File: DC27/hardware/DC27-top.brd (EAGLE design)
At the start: 102.4 x 117.6 mm, 44 parts, among them IC1 PCA9956BTWY

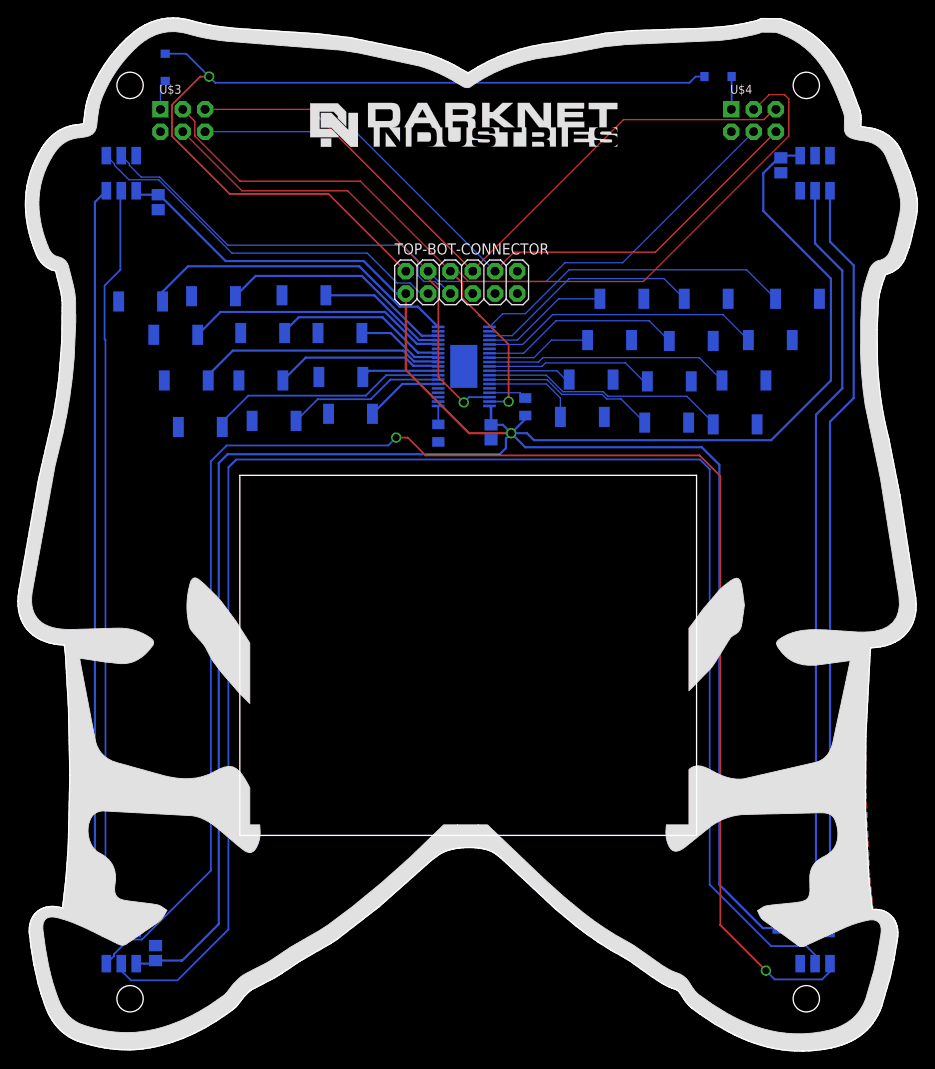
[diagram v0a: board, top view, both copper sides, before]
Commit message: removed apa 102s from top board swapped led driver for atmega4089 put on programming pads bottom board adding paring headers on bottom board added 1206 56 OHM resistors to each LED top board pulled out UPDI pin on top board for programming the atmega chip
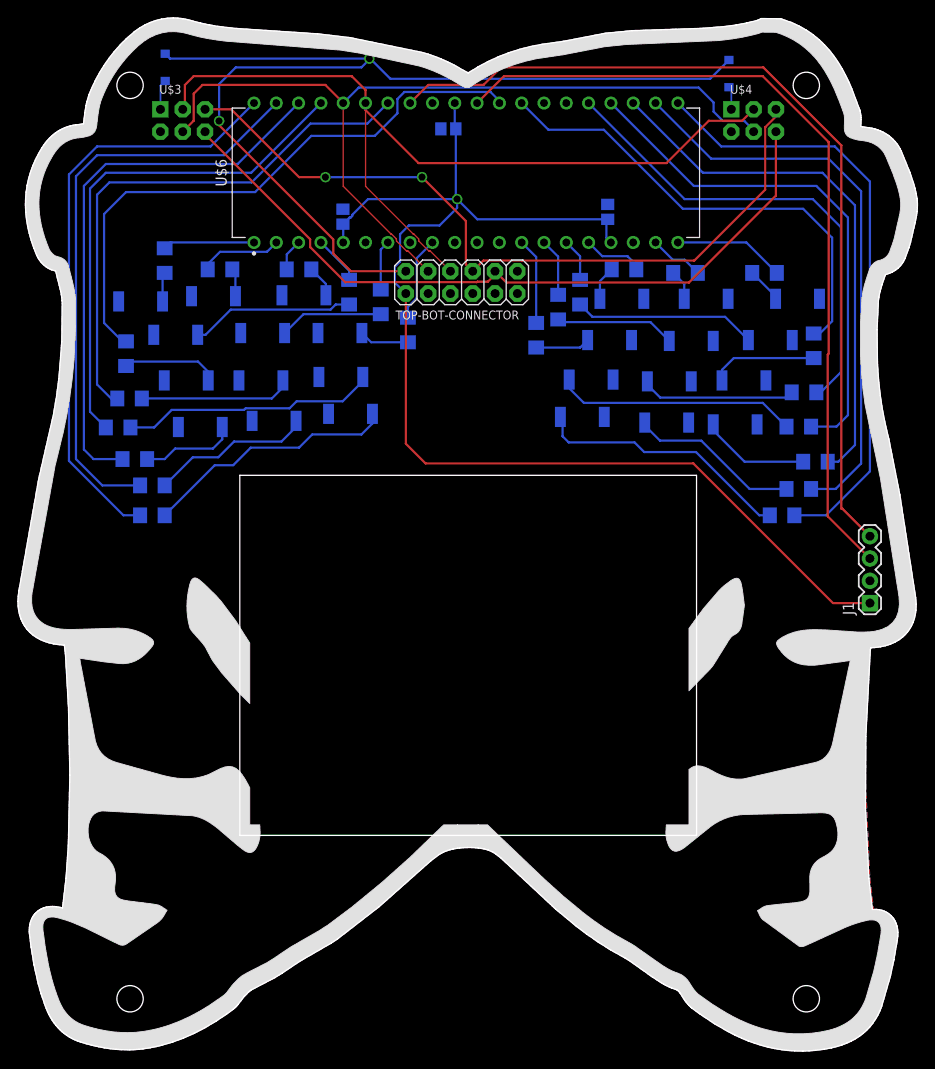
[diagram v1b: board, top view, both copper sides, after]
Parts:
- removed C26, C27, C28, C29: 15 pF, passives:C0805
- removed IC1: PCA9956BTWY, PCA9956BTWY:SOP50P640X110-39N
- removed U$11, U$12, U$13, U$14: APA1025050, leds:APA102_5050
- added C2, C3: 0.1 uF, passives:C0805
- added J1: (no value), connector:1X04
- added R1, R10, R11, R12, R13, R14, R15, R16, R17, R18, R19, R20, R21, R22, R23, R24, R3, R4, R5, R6, R8, R9: 56 R, passives:1206
- added U$6: ATMEGA4809-PFATMEL4809-PF, ICs:DIP1587W58P254L5175H635Q40B
- LED1, LED10, LED11, LED12, LED13, LED14, LED15, LED16, LED17, LED18, LED19, LED2, LED20, LED21, LED22, LED23, LED24, LED3, LED4, LED5, LED6, LED7, LED8, LED9: value (none) -> Amber
- R2: value 10 K -> 56 R; device darknet_parts_library:R0805 -> passives:1206
- R7: value 2 K -> 56 R; device darknet_parts_library:R0805 -> passives:1206
- moved R2 43.4 mm to (15.3, 64.4), turned to 0 degrees
- moved C1 28.4 mm to (67.1, 95.5), turned to 270 degrees
- moved R7 12.2 mm to (44.4, 82.1), turned to 90 degrees
- moved U$5 5.10 mm to (51.8, 100.5), flipped to the bottom
- moved D1 1.23 mm to (81.0, 111.2), turned to 270 degrees
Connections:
- removed net APA102_CLK: TOP-BOT-CONNECTOR.5, U$13.5
- removed net APA102_DATA: TOP-BOT-CONNECTOR.3, U$13.4
- new net N$28: LED6.A, R6.1
- new net N$30: LED18.A, R18.2
- new net N$31: LED1.A, R1.1
- new net N$32: LED2.A, R2.1
- new net N$33: R17.1, U$6.14
- new net N$40: LED22.A, R22.1
- new net N$41: LED19.A, R19.1
- new net N$42: LED21.A, R21.1
- new net N$43: LED20.A, R20.1
- new net N$44: R19.2, U$6.28
- new net N$45: R20.2, U$6.25
- new net N$46: R21.2, U$6.24
- new net N$47: R22.2, U$6.23
- new net N$48: R23.2, U$6.22
- new net N$49: R24.2, U$6.21
- new net N$51: LED3.A, R3.2
- new net PA0: J1.4, U$6.33
- new net PC5: U$6.8
- new net PD1: U$6.10
- new net PD2: U$6.11
- new net PD3: U$6.12
- new net PF3: U$6.26
- new net PF4: U$6.27
- new net UPDI: J1.3, U$6.30
- net GND: now also C2.1, C3.1, J1.2, U$6.18, U$6.32, U$6.6; no longer C26.2, C27.2, C28.2, C29.2, IC1.14, IC1.18, IC1.2, IC1.21, IC1.25, IC1.3, IC1.34, IC1.39, IC1.5, R7.2, U$11.6, U$12.6, U$13.6, U$14.6
- net N$1: now also R9.2, U$6.4; no longer IC1.6, LED1.A
- net N$10: now also R10.1, U$6.3; no longer IC1.16, LED10.A
- net N$11: now also R11.2, U$6.2; no longer IC1.17, LED11.A
- net N$12: now also R12.2, U$6.1; no longer IC1.19, LED12.A
- net N$13: now also R4.2, U$6.37; no longer IC1.20, LED13.A
- net N$14: now also LED5.A, R5.1; no longer IC1.22, LED14.A
- net N$15: now also R5.2, U$6.34; no longer IC1.23, LED15.A
- net N$16: now also R13.1, U$6.20; no longer IC1.24, LED16.A
- net N$17: now also LED13.A, R13.2; no longer IC1.26, LED17.A
- net N$18: now also R14.1, U$6.19; no longer IC1.27, LED18.A
- net N$19: now also LED14.A, R14.2; no longer IC1.28, LED19.A
- net N$2: now also LED9.A, R9.1; no longer IC1.7, LED2.A
- net N$20: now also R15.1, U$6.16; no longer IC1.29, LED20.A
- net N$21: now also LED15.A, R15.2; no longer IC1.30, LED21.A
- net N$22: now also LED17.A, R17.2; no longer IC1.31, LED22.A
- net N$23: now also LED16.A, R16.2; no longer IC1.32, LED23.A
- net N$24: now also R18.1, U$6.13; no longer IC1.33, LED24.A
- net N$27: now also R6.2, U$6.29; no longer U$11.4, U$12.3
- net N$29: now also LED4.A, R4.1; no longer U$12.5, U$14.2
- net N$3: now also R8.2, U$6.7; no longer IC1.8, LED3.A
- net N$34: now also R16.1, U$6.15; no longer U$11.5, U$12.2
- net N$35: now also LED24.A, R24.1; no longer IC1.1, R7.1
- net N$36: now also LED10.A, R10.2; no longer IC1.35, R2.2
- net N$37: now also LED11.A, R11.1; no longer U$12.4, U$14.3
- net N$38: now also LED12.A, R12.1; no longer U$13.3, U$14.4
- net N$39: now also LED23.A, R23.1; no longer U$13.2, U$14.5
- net N$4: now also R7.2, U$6.9; no longer IC1.9, LED4.A
- net N$5: now also R1.2, U$6.40; no longer IC1.10, LED5.A
- net N$6: now also R2.2, U$6.39; no longer IC1.11, LED6.A
- net N$7: now also R3.1, U$6.38; no longer IC1.12, LED7.A
- net N$8: now also R8.1; no longer IC1.13
- net N$9: now also LED7.A, R7.1; no longer IC1.15, LED9.A
- net SCL: now also U$6.36; no longer IC1.36
- net SDA: now also U$6.35; no longer IC1.37
- net VBAT: now also C2.2, C3.2, J1.1, U$6.17, U$6.31, U$6.5; no longer C26.1, C27.1, C28.1, C29.1, IC1.38, R2.1, U$11.1, U$12.1, U$13.1, U$14.1
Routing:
- net N$37: track 191.4 -> 3.20 mm, vias 2 -> 0
- net VBAT: track 321.6 -> 142.2 mm
- net N$29: track 187.7 -> 29.1 mm
- net PA0: track 0.00 -> 100.4 mm
- net UPDI: track 0.00 -> 93.9 mm
- net N$38: track 85.1 -> 3.35 mm
- net N$34: track 86.6 -> 4.91 mm
- net N$49: track 0.00 -> 69.2 mm
- net N$39: track 85.6 -> 19.4 mm
- net N$48: track 0.00 -> 65.5 mm
- net N$47: track 0.00 -> 61.3 mm
- net N$46: track 0.00 -> 59.6 mm
- net N$45: track 0.00 -> 54.8 mm
- net N$44: track 0.00 -> 53.9 mm
- net N$7: track 9.83 -> 63.2 mm
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
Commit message: tweaked position of the led 7 and 8 to be at same Y as the right eye (+/- .1 mm) rerouted trace so it does not go between resistor on bottom board
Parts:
- moved R12 1.48 mm to (16.0, 88.7), turned to 0 degrees
- moved LED8 0.92 mm to (25.2, 79.4)
- moved LED7 0.71 mm to (34.3, 79.6)
- moved LED9 0.60 mm to (15.5, 79.5)
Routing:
- net N$12: track 10.4 -> 14.2 mm
- net N$8: track 11.8 -> 12.4 mm
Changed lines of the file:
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@@
 <layer number="27" name="tValues" color="7" fill="1" visible="no" active="yes"/>
 <layer number="28" name="bValues" color="7" fill="1" visible="no" active="yes"/>
-<layer number="29" name="tStop" color="7" fill="3" visible="no" active="yes"/>
+<layer number="29" name="tStop" color="7" fill="3" visible="yes" active="yes"/>
 <layer number="30" name="bStop" color="7" fill="6" visible="no" active="yes"/>
 <layer number="31" name="tCream" color="7" fill="4" visible="no" active="yes"/>
@@
 <element name="LED5" library="leds" package="GULLWING_LED" value="Amber" x="25.158228125" y="74.850259375" smashed="yes" rot="MR180"/>
 <element name="LED6" library="leds" package="GULLWING_LED" value="Amber" x="16.658228125" y="74.850259375" smashed="yes" rot="MR180"/>
-<element name="LED7" library="leds" package="GULLWING_LED" value="Amber" x="34.158228125" y="80.250259375" smashed="yes" rot="MR180"/>
-<element name="LED8" library="leds" package="GULLWING_LED" value="Amber" x="25.358228125" y="80.250259375" smashed="yes" rot="MR180"/>
-<element name="LED9" library="leds" package="GULLWING_LED" value="Amber" x="15.458228125" y="80.050259375" smashed="yes" rot="MR180"/>
+<element name="LED7" library="leds" package="GULLWING_LED" value="Amber" x="34.258228125" y="79.550259375" smashed="yes" rot="MR180"/>
+<element name="LED8" library="leds" package="GULLWING_LED" value="Amber" x="25.158228125" y="79.350259375" smashed="yes" rot="MR180"/>
+<element name="LED9" library="leds" package="GULLWING_LED" value="Amber" x="15.458228125" y="79.450259375" smashed="yes" rot="MR180"/>
 <element name="LED10" library="leds" package="GULLWING_LED" value="Amber" x="30.058228125" y="84.550259375" smashed="yes" rot="MR180"/>
 <element name="LED11" library="leds" package="GULLWING_LED" value="Amber" x="19.758228125" y="84.450259375" smashed="yes" rot="MR180"/>
@@
 <attribute name="VALUE" x="24.397" y="87.476" size="0.4064" layer="28" rot="MR0"/>
 </element>
-<element name="R12" library="passives" package="1206" value="56 R" x="16.7" y="90" smashed="yes" rot="MR90">
-<attribute name="NAME" x="17.843" y="88.73" size="0.4064" layer="26" rot="MR90"/>
-<attribute name="VALUE" x="15.176" y="88.603" size="0.4064" layer="28" rot="MR90"/>
+<element name="R12" library="passives" package="1206" value="56 R" x="16" y="88.7" smashed="yes" rot="MR0">
+<attribute name="NAME" x="17.27" y="89.843" size="0.4064" layer="26" rot="MR0"/>
+<attribute name="VALUE" x="17.397" y="87.176" size="0.4064" layer="28" rot="MR0"/>
 </element>
 <element name="R13" library="passives" package="1206" value="56 R" x="85" y="88.6" smashed="yes" rot="MR0">
@@
 <contactref element="U$6" pad="1"/>
 <contactref element="R12" pad="2"/>
-<wire x1="17.3625" y1="92.0625" x2="16.7" y2="91.4" width="0.254" layer="16"/>
-<wire x1="26.87" y1="92.0625" x2="17.3625" y2="92.0625" width="0.254" layer="16"/>
+<wire x1="26.87" y1="92.0625" x2="26.8075" y2="92" width="0.1524" layer="16"/>
+<wire x1="26.8075" y1="92" x2="17" y2="92" width="0.1524" layer="16"/>
+<wire x1="17" y1="92" x2="14.6" y2="89.6" width="0.1524" layer="16"/>
+<wire x1="14.6" y1="89.6" x2="14.6" y2="88.7" width="0.1524" layer="16"/>
 </signal>
 <signal name="N$38">
 <contactref element="R12" pad="1"/>
 <contactref element="LED12" pad="A"/>
-<wire x1="16.55" y1="88.45" x2="16.7" y2="88.6" width="0.254" layer="16"/>
-<wire x1="16.458228125" y1="85.350259375" x2="16.458228125" y2="88.358228125" width="0.254" layer="16"/>
-<wire x1="16.458228125" y1="88.358228125" x2="16.55" y2="88.45" width="0.254" layer="16"/>
+<wire x1="16.458228125" y1="85.350259375" x2="16.458228125" y2="86.058228125" width="0.1524" layer="16"/>
+<wire x1="16.458228125" y1="86.058228125" x2="17.4" y2="87" width="0.1524" layer="16"/>
+<wire x1="17.4" y1="87" x2="17.4" y2="88.7" width="0.1524" layer="16"/>
 </signal>
 <signal name="N$11">
@@
 <contactref element="R9" pad="1"/>
 <contactref element="LED9" pad="A"/>
-<wire x1="24.22883125" y1="84.4208625" x2="21.358228125" y2="81.550259375" width="0.254" layer="16"/>
-<wire x1="20.458228125" y1="81.550259375" x2="21.358228125" y2="81.550259375" width="0.254" layer="16"/>
-<wire x1="36.17539375" y1="85" x2="37.7" y2="85" width="0.254" layer="16"/>
-<wire x1="24.22883125" y1="84.4208625" x2="35.59625625" y2="84.4208625" width="0.254" layer="16"/>
-<wire x1="35.59625625" y1="84.4208625" x2="36.17539375" y2="85" width="0.254" layer="16"/>
+<wire x1="25.32883125" y1="84.1208625" x2="22.158228125" y2="80.950259375" width="0.254" layer="16"/>
+<wire x1="20.458228125" y1="80.950259375" x2="22.158228125" y2="80.950259375" width="0.254" layer="16"/>
+<wire x1="37.17539375" y1="85" x2="37.7" y2="85" width="0.254" layer="16"/>
+<wire x1="25.32883125" y1="84.1208625" x2="36.29625625" y2="84.1208625" width="0.254" layer="16"/>
+<wire x1="36.29625625" y1="84.1208625" x2="37.17539375" y2="85" width="0.254" layer="16"/>
 </signal>
 <signal name="N$3">
@@
 <contactref element="R8" pad="1"/>
 <contactref element="LED8" pad="A"/>
-<wire x1="30.358228125" y1="81.750259375" x2="32.50796875" y2="83.9" width="0.254" layer="16"/>
-<wire x1="32.50796875" y1="83.9" x2="41.3" y2="83.9" width="0.254" layer="16"/>
+<wire x1="30.158228125" y1="80.850259375" x2="32.70796875" y2="83.4" width="0.254" layer="16"/>
+<wire x1="40.8" y1="83.4" x2="41.3" y2="83.9" width="0.254" layer="16"/>
+<wire x1="40.8" y1="83.4" x2="32.70796875" y2="83.4" width="0.254" layer="16"/>
 </signal>
 <signal name="N$9">
 <contactref element="R7" pad="1"/>
 <contactref element="LED7" pad="A"/>
-<wire x1="44.4" y1="80.7" x2="40.2084875" y2="80.7" width="0.254" layer="16"/>
-<wire x1="40.2084875" y1="80.7" x2="39.158228125" y2="81.750259375" width="0.254" layer="16"/>
+<wire x1="44.4" y1="80.7" x2="39.6084875" y2="80.7" width="0.254" layer="16"/>
+<wire x1="39.6084875" y1="80.7" x2="39.258228125" y2="81.050259375" width="0.254" layer="16"/>
 </signal>
 <signal name="N$29">
